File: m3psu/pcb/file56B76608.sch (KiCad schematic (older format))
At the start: 48 parts

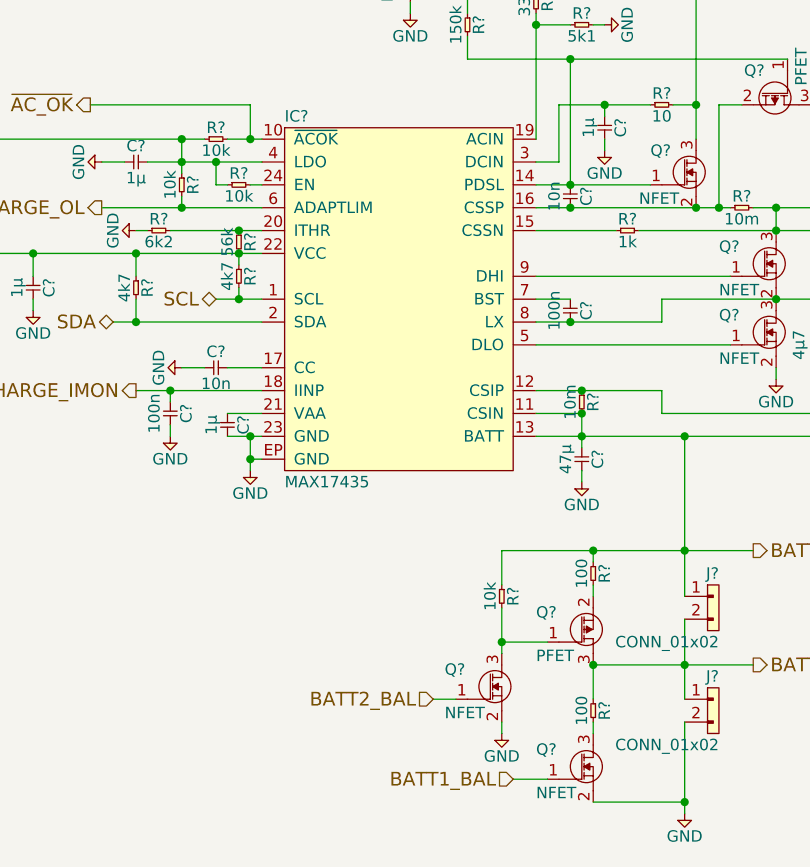
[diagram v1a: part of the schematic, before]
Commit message: Linked the footprints to some parts. Cleaned up a little more of DC/DC Converter.
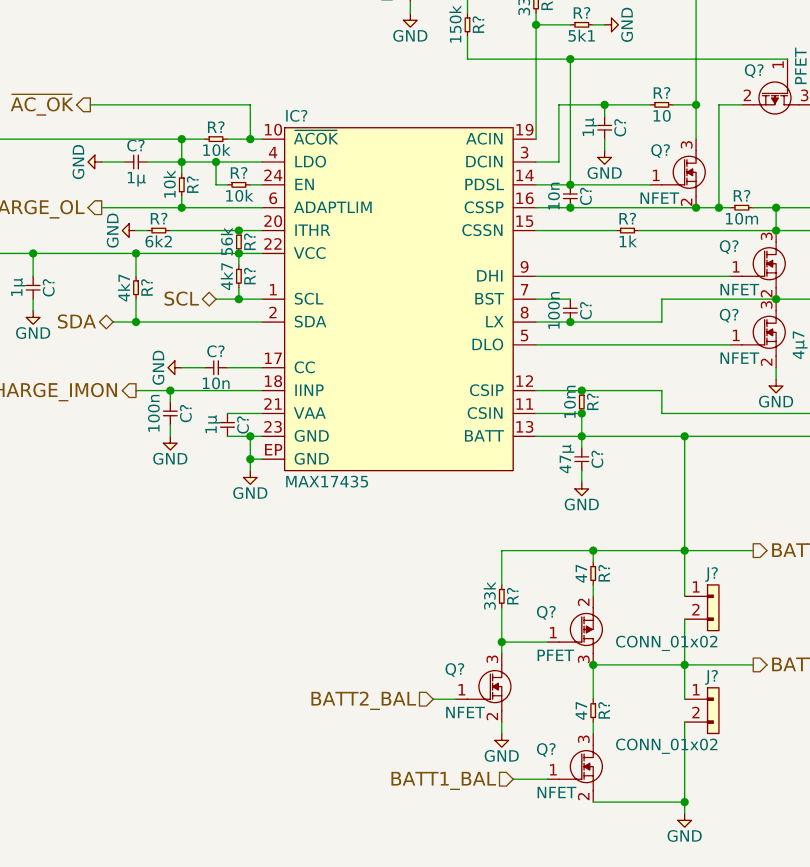
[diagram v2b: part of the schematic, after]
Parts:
- C? (x8), R? (x13): footprint (none) -> agg:0402
- Q? (x2): Farnell (none) -> 2422226
- Q? (x2): Farnell (none) -> 2098274
- Q?: Farnell (none) -> 2335393
- Q? (x3): Farnell (none) -> 2364070
- Q?: Farnell (none) -> 2471947
- R?: footprint (none) -> agg:0402; Power (none) -> 0.1W
- R?: Power (none) -> 0.1W
- R?: Power (none) -> 0.125W
- R? (x2): value 100 -> 47; footprint (none) -> agg:0805; Farnell (none) -> 1750737; Power 1/4 -> 0.5W
- R?: value 10k -> 33k; footprint (none) -> agg:0402
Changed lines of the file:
@@
 F 0 "R?" H 2500 4750 50  0000 C CNN
 F 1 "4k7" H 2500 4650 50  0000 C CNN
-F 2 "" H 2450 4700 50  0001 C CNN
+F 2 "agg:0402" H 2450 4700 50  0001 C CNN
 F 3 "" H 2450 4700 50  0001 C CNN
 	1    2450 4700
@@
 F 0 "R?" H 2950 4700 50  0000 C CNN
 F 1 "4k7" H 2950 4600 50  0000 C CNN
-F 2 "" H 2900 4650 50  0001 C CNN
+F 2 "agg:0402" H 2900 4650 50  0001 C CNN
 F 3 "" H 2900 4650 50  0001 C CNN
 	1    2900 4650
@@
 F 0 "R?" H 4750 4000 50  0000 C CNN
 F 1 "10" H 4750 3900 50  0000 C CNN
-F 2 "" H 4700 3950 50  0001 C CNN
+F 2 "agg:0402" H 4700 3950 50  0001 C CNN
 F 3 "" H 4700 3950 50  0001 C CNN
+F 4 "0.1W" H 4700 3950 60  0001 C CNN "Power"
 	1    4700 3950
 	1    0    0    -1
@@
 F 0 "R?" H 2950 4550 50  0000 C CNN
 F 1 "56k" H 2950 4450 50  0000 C CNN
-F 2 "" H 2900 4500 50  0001 C CNN
+F 2 "agg:0402" H 2900 4500 50  0001 C CNN
 F 3 "" H 2900 4500 50  0001 C CNN
 	1    2900 4500
@@
 F 0 "R?" H 2700 4300 50  0000 C CNN
 F 1 "10k" H 2700 4200 50  0000 C CNN
-F 2 "" H 2650 4250 50  0001 C CNN
+F 2 "agg:0402" H 2650 4250 50  0001 C CNN
 F 3 "" H 2650 4250 50  0001 C CNN
 	1    2650 4250
@@
 F 0 "R?" H 2900 4350 50  0000 C CNN
 F 1 "10k" H 2900 4250 50  0000 C CNN
-F 2 "" H 2850 4300 50  0001 C CNN
+F 2 "agg:0402" H 2850 4300 50  0001 C CNN
 F 3 "" H 2850 4300 50  0001 C CNN
 	1    2850 4300
@@
 F 0 "C?" H 2450 4270 50  0000 C CNN
 F 1 "1µ" H 2450 4130 50  0000 C CNN
-F 2 "" H 2400 4200 50  0001 C CNN
+F 2 "agg:0402" H 2400 4200 50  0001 C CNN
 F 3 "" H 2400 4200 50  0001 C CNN
 	1    2400 4200
@@
 F 0 "R?" H 2800 4150 50  0000 C CNN
 F 1 "10k" H 2800 4050 50  0000 C CNN
-F 2 "" H 2750 4100 50  0001 C CNN
+F 2 "agg:0402" H 2750 4100 50  0001 C CNN
 F 3 "" H 2750 4100 50  0001 C CNN
 	1    2750 4100
@@
 F 0 "C?" H 2900 5370 50  0000 C CNN
 F 1 "1µ" H 2900 5230 50  0000 C CNN
-F 2 "" H 2850 5300 50  0001 C CNN
+F 2 "agg:0402" H 2850 5300 50  0001 C CNN
 F 3 "" H 2850 5300 50  0001 C CNN
 	1    2850 5300
@@
 F 0 "C?" H 2800 5170 50  0000 C CNN
 F 1 "10n" H 2800 5030 50  0000 C CNN
-F 2 "" H 2750 5100 50  0001 C CNN
+F 2 "agg:0402" H 2750 5100 50  0001 C CNN
 F 3 "" H 2750 5100 50  0001 C CNN
 	1    2750 5100
@@
 F 0 "C?" H 2650 5320 50  0000 C CNN
 F 1 "100n" H 2650 5180 50  0000 C CNN
-F 2 "" H 2600 5250 50  0001 C CNN
+F 2 "agg:0402" H 2600 5250 50  0001 C CNN
 F 3 "" H 2600 5250 50  0001 C CNN
 	1    2600 5250
@@
 F 0 "C?" H 2050 4770 50  0000 C CNN
 F 1 "1µ" H 2050 4630 50  0000 C CNN
-F 2 "" H 2000 4700 50  0001 C CNN
+F 2 "agg:0402" H 2000 4700 50  0001 C CNN
 F 3 "" H 2000 4700 50  0001 C CNN
 	1    2000 4700
@@
 F 0 "R?" H 1650 4350 50  0000 C CNN
 F 1 "10" H 1650 4250 50  0000 C CNN
-F 2 "" H 1600 4300 50  0001 C CNN
+F 2 "agg:0402" H 1600 4300 50  0001 C CNN
 F 3 "" H 1600 4300 50  0001 C CNN
 	1    1600 4300
@@
 F 0 "R?" H 2550 4550 50  0000 C CNN
 F 1 "6k2" H 2550 4450 50  0000 C CNN
-F 2 "" H 2500 4500 50  0001 C CNN
+F 2 "agg:0402" H 2500 4500 50  0001 C CNN
 F 3 "" H 2500 4500 50  0001 C CNN
 	1    2500 4500
@@
 F 2 "" H 4400 5200 50  0001 C CNN
 F 3 "" H 4400 5200 50  0001 C CNN
+F 4 "0.1W" H 4400 5200 60  0001 C CNN "Power"
 	1    4400 5200
 	0    1    1    0
@@
 F 0 "C?" H 4400 4870 50  0000 C CNN
 F 1 "100n" H 4400 4730 50  0000 C CNN
-F 2 "" H 4350 4800 50  0001 C CNN
+F 2 "agg:0402" H 4350 4800 50  0001 C CNN
 F 3 "" H 4350 4800 50  0001 C CNN
 	1    4350 4800
@@
 F 2 "" H 5250 4600 50  0001 C CNN
 F 3 "" H 5250 4600 50  0001 C CNN
+F 4 "2422226" H 5250 4600 60  0001 C CNN "Farnell"
 	1    5250 4600
 	1    0    0    -1
@@
 F 2 "" H 5250 4900 50  0001 C CNN
 F 3 "" H 5250 4900 50  0001 C CNN
+F 4 "2422226" H 5250 4900 60  0001 C CNN "Farnell"
 	1    5250 4900
 	1    0    0    -1
@@
 F 2 "" H 4900 4200 50  0001 C CNN
 F 3 "" H 4900 4200 50  0001 C CNN
+F 4 "2098274" H 4900 4200 60  0001 C CNN "Farnell"
 	1    4900 4200
 	1    0    0    -1
@@
 F 2 "" H 4200 3250 50  0001 C CNN
 F 3 "" H 4200 3250 50  0001 C CNN
+F 4 "2098274" H 4200 3250 60  0001 C CNN "Farnell"
 	1    4200 3250
 	1    0    0    1
@@
 F 2 "" H 5050 4400 50  0001 C CNN
 F 3 "" H 5050 4400 50  0001 C CNN
+F 4 "0.125W" H 5050 4400 60  0001 C CNN "Power"
 	1    5050 4400
 	1    0    0    -1
@@
 F 2 "" H 4450 6200 50  0001 C CNN
 F 3 "" H 4450 6200 50  0001 C CNN
+F 4 "2335393" H 4450 6200 60  0001 C CNN "Farnell"
 	1    4450 6200
 	1    0    0    -1
@@
 F 2 "" H 4450 6800 50  0001 C CNN
 F 3 "" H 4450 6800 50  0001 C CNN
+F 4 "2364070" H 4450 6800 60  0001 C CNN "Farnell"
 	1    4450 6800
 	1    0    0    -1
@@
 P 4450 5950
 F 0 "R?" H 4500 6000 50  0000 C CNN
-F 1 "100" H 4500 5900 50  0000 C CNN
-F 2 "" H 4450 5950 50  0001 C CNN
+F 1 "47" H 4500 5900 50  0000 C CNN
+F 2 "agg:0805" H 4450 5950 50  0001 C CNN
 F 3 "" H 4450 5950 50  0001 C CNN
-F 4 "1/4" H 4450 5950 60  0001 C CNN "Power"
+F 4 "1750737" H 4450 5950 60  0001 C CNN "Farnell"
+F 5 "0.5W" H 4450 5950 60  0001 C CNN "Power"
 	1    4450 5950
 	0    1    1    0
@@
 P 4450 6550
 F 0 "R?" H 4500 6600 50  0000 C CNN
-F 1 "100" H 4500 6500 50  0000 C CNN
-F 2 "" H 4450 6550 50  0001 C CNN
+F 1 "47" H 4500 6500 50  0000 C CNN
+F 2 "agg:0805" H 4450 6550 50  0001 C CNN
 F 3 "" H 4450 6550 50  0001 C CNN
-F 4 "1/4" H 4450 6550 60  0001 C CNN "Power"
+F 4 "1750737" H 4450 6550 60  0001 C CNN "Farnell"
+F 5 "0.5W" H 4450 6550 60  0001 C CNN "Power"
 	1    4450 6550
 	0    1    1    0
@@
 F 2 "" H 4050 6450 50  0001 C CNN
 F 3 "" H 4050 6450 50  0001 C CNN
+F 4 "2364070" H 4050 6450 60  0001 C CNN "Farnell"
 	1    4050 6450
 	1    0    0    -1
@@
 P 4050 6050
 F 0 "R?" H 4100 6100 50  0000 C CNN
-F 1 "10k" H 4100 6000 50  0000 C CNN
-F 2 "" H 4050 6050 50  0001 C CNN
+F 1 "33k" H 4100 6000 50  0000 C CNN
+F 2 "agg:0402" H 4050 6050 50  0001 C CNN
 F 3 "" H 4050 6050 50  0001 C CNN
 	1    4050 6050
@@
 F 2 "" H 3750 3300 50  0001 C CNN
 F 3 "" H 3750 3300 50  0001 C CNN
+F 4 "2364070" V 3750 3300 60  0001 C CNN "Farnell"
 	1    3750 3300
 	0    1    -1   0
@@
 F 0 "R?" H 3700 3200 50  0000 C CNN
 F 1 "2M" H 3700 3100 50  0000 C CNN
-F 2 "" H 3650 3150 50  0001 C CNN
+F 2 "agg:0402" H 3650 3150 50  0001 C CNN
 F 3 "" H 3650 3150 50  0001 C CNN
 	1    3650 3150
@@
 F 0 "R?" H 3950 3600 50  0000 C CNN
 F 1 "150k" H 3950 3500 50  0000 C CNN
-F 2 "" H 3900 3550 50  0001 C CNN
+F 2 "agg:0402" H 3900 3550 50  0001 C CNN
 F 3 "" H 3900 3550 50  0001 C CNN
 	1    3900 3550
@@
 F 0 "C?" H 4400 4370 50  0000 C CNN
 F 1 "10n" H 4400 4230 50  0000 C CNN
-F 2 "" H 4350 4300 50  0001 C CNN
+F 2 "agg:0402" H 4350 4300 50  0001 C CNN
 F 3 "" H 4350 4300 50  0001 C CNN
 	1    4350 4300
@@
 F 0 "C?" H 4550 4070 50  0000 C CNN
 F 1 "1µ" H 4550 3930 50  0000 C CNN
-F 2 "" H 4500 4000 50  0001 C CNN
+F 2 "agg:0402" H 4500 4000 50  0001 C CNN
 F 3 "" H 4500 4000 50  0001 C CNN
 	1    4500 4000
@@
 F 2 "" H 5200 3950 50  0001 C CNN
 F 3 "" H 5200 3950 50  0001 C CNN
+F 4 "2471947" V 5200 3950 60  0001 C CNN "Farnell"
 	1    5200 3950
 	0    -1   1    0
@@
 F 0 "R?" H 4250 3500 50  0000 C CNN
 F 1 "33k" H 4250 3400 50  0000 C CNN
-F 2 "" H 4200 3450 50  0001 C CNN
+F 2 "agg:0402" H 4200 3450 50  0001 C CNN
 F 3 "" H 4200 3450 50  0001 C CNN
 	1    4200 3450
@@
 F 0 "R?" H 4400 3650 50  0000 C CNN
 F 1 "5k1" H 4400 3550 50  0000 C CNN
-F 2 "" H 4350 3600 50  0001 C CNN
+F 2 "agg:0402" H 4350 3600 50  0001 C CNN
 F 3 "" H 4350 3600 50  0001 C CNN
 	1    4350 3600
@@
 Connection ~ 2800 4200
 Wire Wire Line
-	2800 4200 2800 4300
+	2800 4300 2800 4200
 Wire Wire Line
 	2950 4300 3000 4300
@@
 F 0 "R?" H 4600 4550 50  0000 C CNN
 F 1 "1k" H 4600 4450 50  0000 C CNN
-F 2 "" H 4550 4500 50  0001 C CNN
+F 2 "agg:0402" H 4550 4500 50  0001 C CNN
 F 3 "" H 4550 4500 50  0001 C CNN
 	1    4550 4500

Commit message: Finished up Li-ion charger and power OR. Update agg-kicad.
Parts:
- C? (x4): Farnell (none) -> 2218855
- C? (x2): Farnell (none) -> 2210793
- C? (x2): Farnell (none) -> 2496811
- C?: footprint (none) -> agg:0402; Farnell (none) -> 2496811
- C?: value C -> 22n; footprint (none) -> ag:0402; Farnell (none) -> 2210825
- C?: value C -> 22n; footprint (none) -> agg:0402; Farnell (none) -> 2210825
- L?: footprint (none) -> agg:SRP5030T
- Q? (x2): Farnell (none) -> 2098274
- R? (x2): Farnell (none) -> 2447187
- R?: Farnell (none) -> 1738824; Power 0.1W -> 0.125W
- R?: Farnell (none) -> 2447198
- R? (x3): Farnell (none) -> 2447096
- R?: Farnell (none) -> 2447120
- R?: Farnell (none) -> 2331559
- R? (x2): footprint (none) -> agg:0603; Farnell (none) -> 2503038
- R? (x2): Farnell (none) -> 2447160
- R?: Farnell (none) -> 1458762
- R?: Farnell (none) -> 2447110
- R?: Farnell (none) -> 2447201
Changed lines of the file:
@@
 F 2 "agg:0402" H 2450 4700 50  0001 C CNN
 F 3 "" H 2450 4700 50  0001 C CNN
+F 4 "2447187" H 2450 4700 60  0001 C CNN "Farnell"
 	1    2450 4700
 	0    1    1    0
@@
 F 2 "agg:0402" H 2900 4650 50  0001 C CNN
 F 3 "" H 2900 4650 50  0001 C CNN
+F 4 "2447187" H 2900 4650 60  0001 C CNN "Farnell"
 	1    2900 4650
 	0    1    1    0
@@
 F 2 "agg:0402" H 4700 3950 50  0001 C CNN
 F 3 "" H 4700 3950 50  0001 C CNN
-F 4 "0.1W" H 4700 3950 60  0001 C CNN "Power"
+F 4 "0.125W" H 4700 3950 60  0001 C CNN "Power"
+F 5 "1738824" H 4700 3950 60  0001 C CNN "Farnell"
 	1    4700 3950
 	1    0    0    -1
@@
 F 2 "agg:0402" H 2900 4500 50  0001 C CNN
 F 3 "" H 2900 4500 50  0001 C CNN
+F 4 "2447198" H 2900 4500 60  0001 C CNN "Farnell"
 	1    2900 4500
 	0    1    1    0
@@
 F 2 "agg:0402" H 2650 4250 50  0001 C CNN
 F 3 "" H 2650 4250 50  0001 C CNN
+F 4 "2447096" H 2650 4250 60  0001 C CNN "Farnell"
 	1    2650 4250
 	0    1    1    0
@@
 F 2 "agg:0402" H 2850 4300 50  0001 C CNN
 F 3 "" H 2850 4300 50  0001 C CNN
+F 4 "2447096" H 2850 4300 60  0001 C CNN "Farnell"
 	1    2850 4300
 	1    0    0    -1
@@
 F 2 "agg:0402" H 2400 4200 50  0001 C CNN
 F 3 "" H 2400 4200 50  0001 C CNN
+F 4 "2218855" H 2400 4200 60  0001 C CNN "Farnell"
 	1    2400 4200
 	1    0    0    -1
@@
 F 2 "agg:0402" H 2750 4100 50  0001 C CNN
 F 3 "" H 2750 4100 50  0001 C CNN
+F 4 "2447096" H 2750 4100 60  0001 C CNN "Farnell"
 	1    2750 4100
 	1    0    0    -1
@@
 F 2 "agg:0402" H 2850 5300 50  0001 C CNN
 F 3 "" H 2850 5300 50  0001 C CNN
+F 4 "2218855" H 2850 5300 60  0001 C CNN "Farnell"
 	1    2850 5300
 	0    1    1    0
@@
 F 2 "agg:0402" H 2750 5100 50  0001 C CNN
 F 3 "" H 2750 5100 50  0001 C CNN
+F 4 "2210793" H 2750 5100 60  0001 C CNN "Farnell"
 	1    2750 5100
 	1    0    0    -1
@@
 F 2 "agg:0402" H 2600 5250 50  0001 C CNN
 F 3 "" H 2600 5250 50  0001 C CNN
+F 4 "2496811" H 2600 5250 60  0001 C CNN "Farnell"
 	1    2600 5250
 	0    1    1    0
@@
 F 2 "agg:0402" H 2000 4700 50  0001 C CNN
 F 3 "" H 2000 4700 50  0001 C CNN
+F 4 "2218855" H 2000 4700 60  0001 C CNN "Farnell"
 	1    2000 4700
 	0    1    1    0
@@
 F 2 "agg:0402" H 2500 4500 50  0001 C CNN
 F 3 "" H 2500 4500 50  0001 C CNN
+F 4 "2331559" H 2500 4500 60  0001 C CNN "Farnell"
 	1    2500 4500
 	1    0    0    -1
@@
 F 0 "R?" H 4450 5250 50  0000 C CNN
 F 1 "10m" H 4450 5150 50  0000 C CNN
-F 2 "" H 4400 5200 50  0001 C CNN
+F 2 "agg:0603" H 4400 5200 50  0001 C CNN
 F 3 "" H 4400 5200 50  0001 C CNN
 F 4 "0.1W" H 4400 5200 60  0001 C CNN "Power"
+F 5 "2503038" H 4400 5200 60  0001 C CNN "Farnell"
 	1    4400 5200
 	0    1    1    0
@@
 F 2 "agg:0402" H 4350 4800 50  0001 C CNN
 F 3 "" H 4350 4800 50  0001 C CNN
+F 4 "2496811" H 4350 4800 60  0001 C CNN "Farnell"
 	1    4350 4800
 	0    1    1    0
@@
 F 0 "C?" H 7100 2020 50  0000 C CNN
 F 1 "100n" H 7100 1880 50  0000 C CNN
-F 2 "" H 7050 1950 50  0001 C CNN
+F 2 "agg:0402" H 7050 1950 50  0001 C CNN
 F 3 "" H 7050 1950 50  0001 C CNN
+F 4 "2496811" H 7050 1950 60  0001 C CNN "Farnell"
 	1    7050 1950
 	0    1    1    0
@@
 P 9200 1450
 F 0 "C?" H 9250 1520 50  0000 C CNN
-F 1 "C" H 9250 1380 50  0000 C CNN
-F 2 "" H 9200 1450 50  0001 C CNN
+F 1 "22n" H 9250 1380 50  0000 C CNN
+F 2 "ag:0402" H 9200 1450 50  0001 C CNN
 F 3 "" H 9200 1450 50  0001 C CNN
+F 4 "2210825" H 9200 1450 60  0001 C CNN "Farnell"
 	1    9200 1450
 	1    0    0    -1
@@
 P 9200 1950
 F 0 "C?" H 9250 2020 50  0000 C CNN
-F 1 "C" H 9250 1880 50  0000 C CNN
-F 2 "" H 9200 1950 50  0001 C CNN
+F 1 "22n" H 9250 1880 50  0000 C CNN
+F 2 "agg:0402" H 9200 1950 50  0001 C CNN
 F 3 "" H 9200 1950 50  0001 C CNN
+F 4 "2210825" H 9200 1950 60  0001 C CNN "Farnell"
 	1    9200 1950
 	1    0    0    -1
@@
 F 0 "L?" H 5450 5000 50  0000 C CNN
 F 1 "4µ7" H 5450 4900 50  0000 C CNN
-F 2 "" H 5400 4950 50  0001 C CNN
+F 2 "agg:SRP5030T" H 5400 4950 50  0001 C CNN
 F 3 "" H 5400 4950 50  0001 C CNN
 F 4 "2309887" H 5400 4950 60  0001 C CNN "Farnell"
@@
 F 0 "R?" H 5100 4450 50  0000 C CNN
 F 1 "10m" H 5100 4350 50  0000 C CNN
-F 2 "" H 5050 4400 50  0001 C CNN
+F 2 "agg:0603" H 5050 4400 50  0001 C CNN
 F 3 "" H 5050 4400 50  0001 C CNN
 F 4 "0.125W" H 5050 4400 60  0001 C CNN "Power"
+F 5 "2503038" H 5050 4400 60  0001 C CNN "Farnell"
 	1    5050 4400
 	1    0    0    -1
@@
 F 2 "agg:0402" H 4050 6050 50  0001 C CNN
 F 3 "" H 4050 6050 50  0001 C CNN
+F 4 "2447160" H 4050 6050 60  0001 C CNN "Farnell"
 	1    4050 6050
 	0    1    1    0
@@
 F 2 "" H 9750 1550 50  0001 C CNN
 F 3 "" H 9750 1550 50  0001 C CNN
+F 4 "2098274" H 9750 1550 60  0001 C CNN "Farnell"
 	1    9750 1550
 	1    0    0    -1
@@
 F 2 "" H 9750 2250 50  0001 C CNN
 F 3 "" H 9750 2250 50  0001 C CNN
+F 4 "2098274" H 9750 2250 60  0001 C CNN "Farnell"
 	1    9750 2250
 	1    0    0    1
@@
 F 2 "agg:0402" H 3650 3150 50  0001 C CNN
 F 3 "" H 3650 3150 50  0001 C CNN
+F 4 "1458762" H 3650 3150 60  0001 C CNN "Farnell"
 	1    3650 3150
 	1    0    0    -1
@@
 F 2 "agg:0402" H 3900 3550 50  0001 C CNN
 F 3 "" H 3900 3550 50  0001 C CNN
+F 4 "2447110" H 3900 3550 60  0001 C CNN "Farnell"
 	1    3900 3550
 	0    1    1    0
@@
 F 2 "agg:0402" H 4350 4300 50  0001 C CNN
 F 3 "" H 4350 4300 50  0001 C CNN
+F 4 "2210793" H 4350 4300 60  0001 C CNN "Farnell"
 	1    4350 4300
 	0    1    1    0
@@
 F 2 "agg:0402" H 4500 4000 50  0001 C CNN
 F 3 "" H 4500 4000 50  0001 C CNN
+F 4 "2218855" H 4500 4000 60  0001 C CNN "Farnell"
 	1    4500 4000
 	0    1    1    0
@@
 F 2 "agg:0402" H 4200 3450 50  0001 C CNN
 F 3 "" H 4200 3450 50  0001 C CNN
+F 4 "2447160" H 4200 3450 60  0001 C CNN "Farnell"
 	1    4200 3450
 	0    1    1    0
@@
 F 2 "agg:0402" H 4350 3600 50  0001 C CNN
 F 3 "" H 4350 3600 50  0001 C CNN
+F 4 "2447201" H 4350 3600 60  0001 C CNN "Farnell"
 	1    4350 3600
 	1    0    0    -1
@@
 F 2 "agg:0402" H 4550 4500 50  0001 C CNN
 F 3 "" H 4550 4500 50  0001 C CNN
+F 4 "2447120" H 4550 4500 60  0001 C CNN "Farnell"
 	1    4550 4500
 	1    0    0    -1

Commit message: Finished touchup. All components have Farnell Numbers. Need help for creating A/B footprints before routing can begin.
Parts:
- R?: Farnell (none) -> 1738824
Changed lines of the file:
@@
 F 2 "agg:0402" H 1600 4300 50  0001 C CNN
 F 3 "" H 1600 4300 50  0001 C CNN
+F 4 "1738824" H 1600 4300 60  0001 C CNN "Farnell"
 	1    1600 4300
 	0    1    1    0

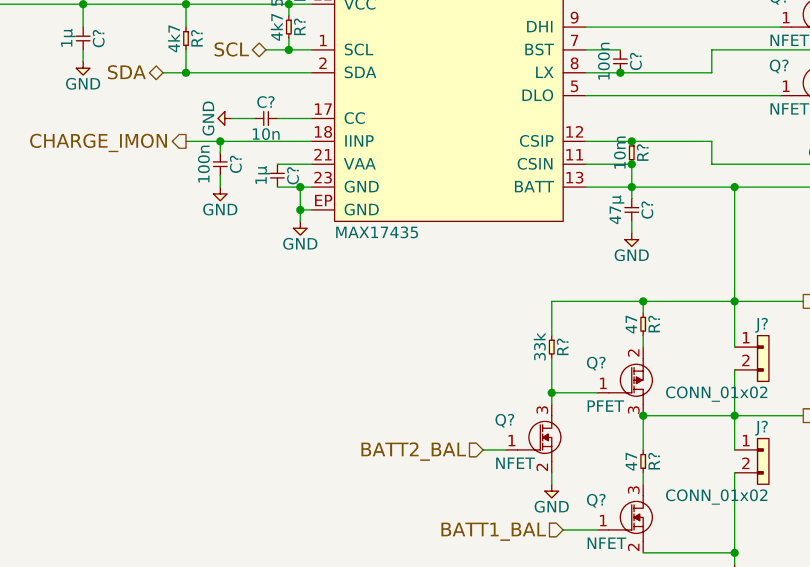
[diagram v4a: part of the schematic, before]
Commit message: Added address text to Li-ion Charger. Updated README.md.
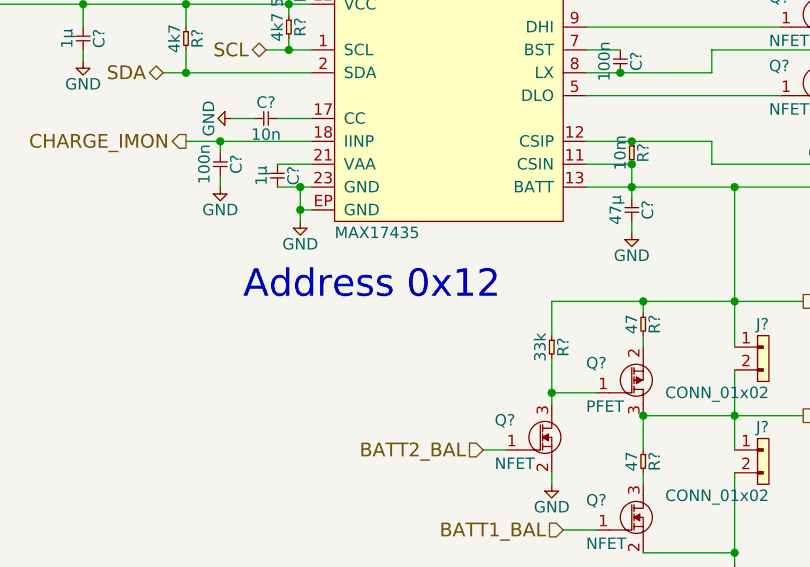
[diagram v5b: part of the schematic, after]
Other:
- note added: "Address 0x12"
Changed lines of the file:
@@
 	1    0    0    -1
 $EndComp
+Text Notes 2700 5900 0    120  ~ 0
+Address 0x12
 $EndSCHEMATC
